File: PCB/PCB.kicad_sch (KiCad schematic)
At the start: 17 parts, among them J1 Conn_01x06_Female, J3 DB25_Receptacle_MountingHoles, U13 74HC165, U15 LT3042xMSE, U16 74HC165

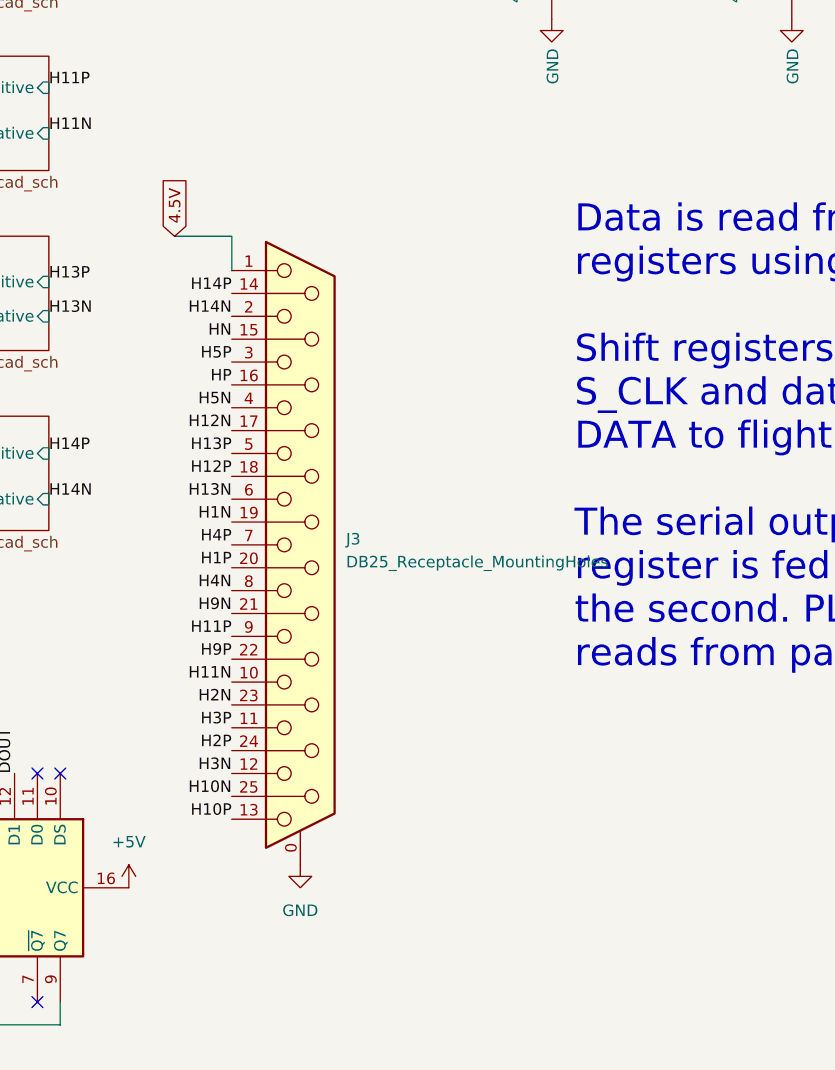
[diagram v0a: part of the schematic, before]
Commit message: Beginning new layout
As I am placing components on the board, I am getting the impression that 70 mm by 70 mm is too small of a board for what I am attempting. The through hole connectors that I am looking at are too big to allow 2 hx711 adc to fit alongside them in their current setup. At some point, I will have to go back to the circular pcb design but learn my lessons from it and set it up with the hx711's at 45 degrees and I may have enough room.
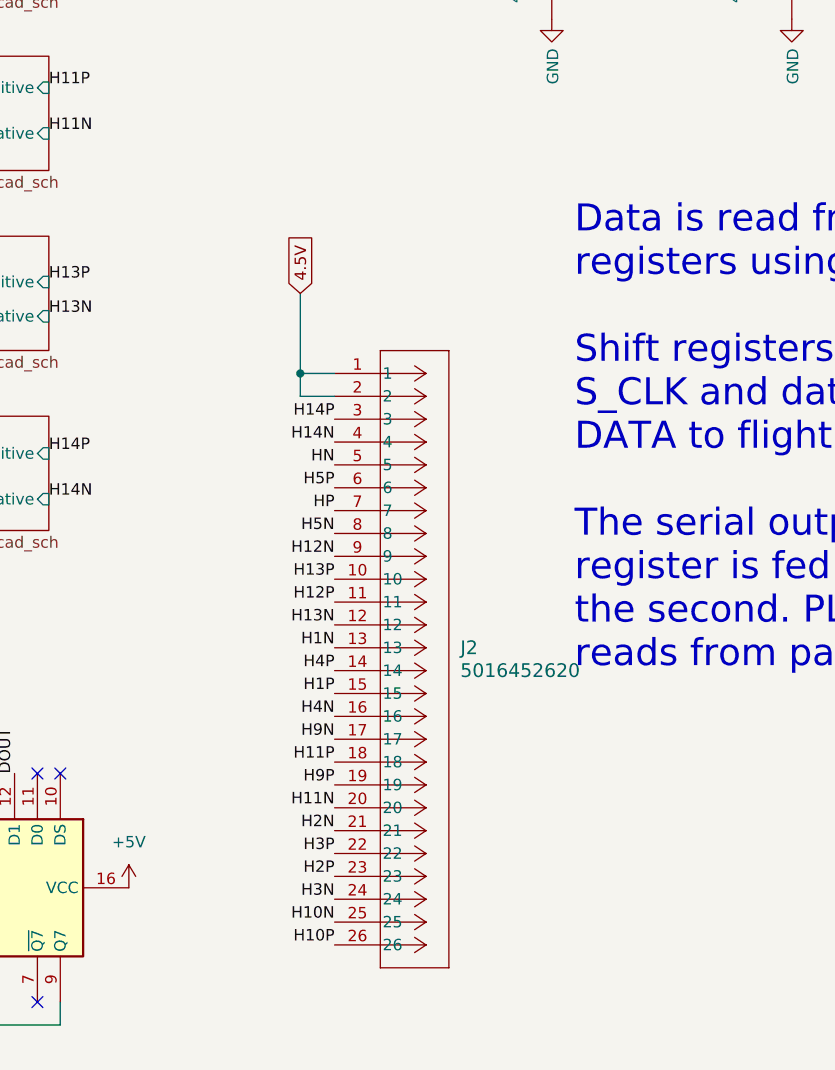
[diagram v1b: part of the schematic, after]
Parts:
- removed J3: DB25_Receptacle_MountingHoles, Connector_Dsub:DSUB-25_Female_Vertical_P2.77x2.84mm_MountingHoles, symbol Connector:DB25_Receptacle_MountingHoles
- added J2: 5016452620, Library:CON_5016452620_MOL, symbol 2024-03-05_00-01-19:5016452620
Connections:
- net 4.5V: now also J2.1, J2.2
- net H10N: now also J2.25
- net H10P: now also J2.26
- net H11N: now also J2.20
- net H11P: now also J2.18
- net H12N: now also J2.9
- net H12P: now also J2.11
- net H13N: now also J2.12
- net H13P: now also J2.10
- net H14N: now also J2.4
- net H14P: now also J2.3
- net H1N: now also J2.13
- net H1P: now also J2.15
- net H2N: now also J2.21
- net H2P: now also J2.23
- net H3N: now also J2.24
- net H3P: now also J2.22
- net H4N: now also J2.16
- net H4P: now also J2.14
- net H5N: now also J2.8
- net H5P: now also J2.6
- net H9N: now also J2.17
- net H9P: now also J2.19
- net HN: now also J2.5
- net HP: now also J2.7

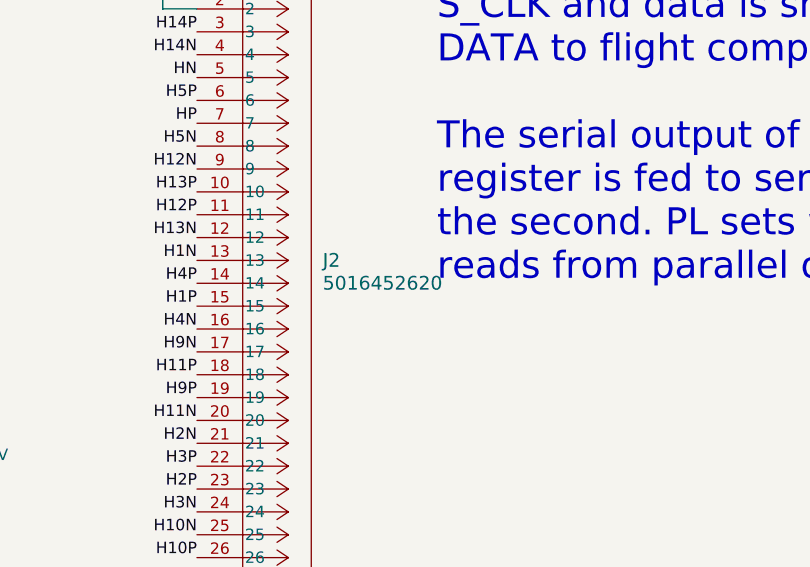
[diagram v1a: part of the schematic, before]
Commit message: Imported other downloaded connector
Imported other downloaded through hole connector to compare sizes with another one, even though they will be on different sides from the top of the board. I'm just concerned that I won't be able to work this board setup.
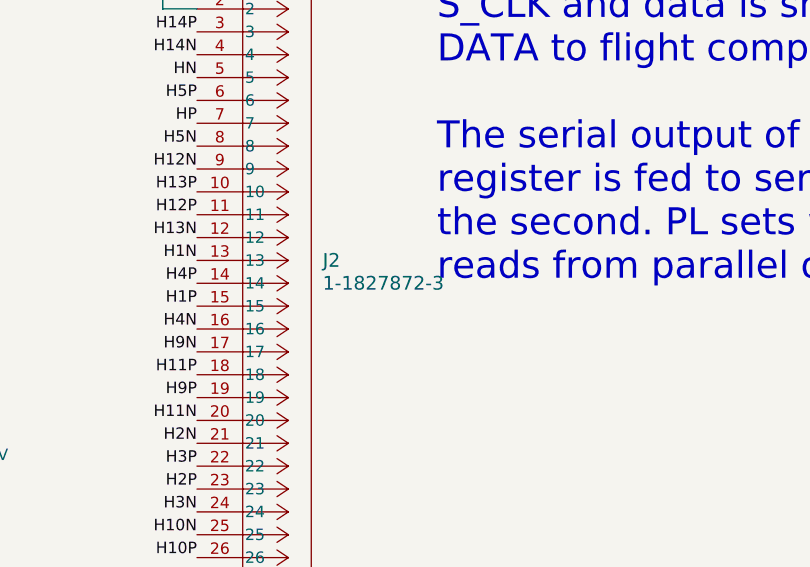
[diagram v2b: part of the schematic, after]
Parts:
- removed J2: 5016452620, Library:CON_5016452620_MOL, symbol 2024-03-05_00-01-19:5016452620
- added J2: 1-1827872-3, Library:CONN_1-1827872-3_TYC, symbol 2024-03-04_23-53-42:1-1827872-3
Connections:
- net 4.5V: now also J2.1, J2.2
- net H10N: now also J2.25
- net H10P: now also J2.26
- net H11N: now also J2.20
- net H11P: now also J2.18
- net H12N: now also J2.9
- net H12P: now also J2.11
- net H13N: now also J2.12
- net H13P: now also J2.10
- net H14N: now also J2.4
- net H14P: now also J2.3
- net H1N: now also J2.13
- net H1P: now also J2.15
- net H2N: now also J2.21
- net H2P: now also J2.23
- net H3N: now also J2.24
- net H3P: now also J2.22
- net H4N: now also J2.16
- net H4P: now also J2.14
- net H5N: now also J2.8
- net H5P: now also J2.6
- net H9N: now also J2.17
- net H9P: now also J2.19
- net HN: now also J2.5
- net HP: now also J2.7
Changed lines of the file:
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@@
-	)
-	(symbol
-		(lib_id "2024-03-05_00-01-19:5016452620")
-		(at 144.78 120.65 0)
-		(unit 1)
-		(exclude_from_sim no)
-		(in_bom yes)
-		(on_board yes)
-		(dnp no)
-		(fields_autoplaced yes)
-		(property "Reference" "J2"
-			(at 158.75 151.1299 0)
-			(effects
-				(font
-					(size 1.524 1.524)
-				)
-				(justify left)
-			)
-		)
-		(property "Value" "5016452620"
-			(at 158.75 153.6699 0)
-			(effects
-				(font
-					(size 1.524 1.524)
-				)
-				(justify left)
-			)
-		)
-		(property "Footprint" "Library:CON_5016452620_MOL"
-			(at 144.78 120.65 0)
-			(effects
-				(font
-					(size 1.27 1.27)
-					(italic yes)
-				)
-				(hide yes)
-			)
-		)
-		(property "Datasheet" "5016452620"
-			(at 144.78 120.65 0)
-			(effects
-				(font
-					(size 1.27 1.27)
-					(italic yes)
-				)
-				(hide yes)
-			)
-		)
-		(property "Description" ""
-			(at 144.78 120.65 0)
-			(effects
-				(font
-					(size 1.27 1.27)
-				)
-				(hide yes)
-			)
-		)
-		(pin "22"
-		)
-		(pin "13"
-		)
-		(pin "25"
-		)
-		(pin "20"
-		)
-		(pin "9"
-		)
-		(pin "21"
-		)
-		(pin "17"
-		)
-		(pin "14"
-		)
-		(pin "7"
-		)
-		(pin "26"
-		)
-		(pin "6"
-		)
-		(pin "18"
-		)
-		(pin "2"
-		)
-		(pin "5"
-		)
-		(pin "19"
-		)
-		(pin "15"
-		)
-		(pin "1"
-		)
-		(pin "8"
-		)
-		(pin "3"
-		)
-		(pin "4"
-		)
-		(pin "11"
-		)
-		(pin "24"
-		)
-		(pin "23"
-		)
-		(pin "10"
-		)
-		(pin "16"
-		)
-		(pin "12"
-		)
-		(instances
-			(project "PCB"
-				(path "/b6270a28-e0d9-4655-a18a-03dbf007b940"
-					(reference "J2")
-					(unit 1)
-				)
-			)
-		)
 	)
 	(symbol
@@
 					(unit 1)
 				)
+			)
+		)
+	)
+	(symbol
+		(lib_id "2024-03-04_23-53-42:1-1827872-3")
+		(at 144.78 120.65 0)
+		(unit 1)
+		(exclude_from_sim no)
+		(in_bom yes)
+		(on_board yes)
+		(dnp no)
+		(fields_autoplaced yes)
+		(property "Reference" "J2"
+			(at 158.75 151.1299 0)
+			(effects
+				(font
+					(size 1.524 1.524)
+				)
+				(justify left)
+			)
+		)
+		(property "Value" "1-1827872-3"
+			(at 158.75 153.6699 0)
+			(effects
+				(font
+					(size 1.524 1.524)
+				)
+				(justify left)
+			)
+		)
+		(property "Footprint" "Library:CONN_1-1827872-3_TYC"
+			(at 144.78 120.65 0)
+			(effects
+				(font
+					(size 1.27 1.27)
+					(italic yes)
+				)
+				(hide yes)
+			)
+		)
+		(property "Datasheet" "1-1827872-3"
+			(at 144.78 120.65 0)
+			(effects
+				(font
+					(size 1.27 1.27)
+					(italic yes)
+				)
+				(hide yes)
+			)
+		)
+		(property "Description" ""
+			(at 144.78 120.65 0)
+			(effects
+				(font
+					(size 1.27 1.27)
+				)
+				(hide yes)
+			)
+		)
+		(pin "14"
+		)
+		(pin "15"
+		)
+		(pin "12"
+		)
+		(pin "2"
+		)
+		(pin "1"
+		)
+		(pin "17"
+		)
+		(pin "11"
+		)
+		(pin "22"
+		)
+		(pin "25"
+		)
+		(pin "13"
+		)
+		(pin "24"
+		)
+		(pin "7"
+		)
+		(pin "23"
+		)
+		(pin "10"
+		)
+		(pin "3"
+		)
+		(pin "16"
+		)
+		(pin "18"
+		)
+		(pin "19"
+		)
+		(pin "26"
+		)
+		(pin "4"
+		)
+		(pin "5"
+		)
+		(pin "8"
+		)
+		(pin "20"
+		)
+		(pin "21"
+		)
+		(pin "9"
+		)
+		(pin "6"
+		)
+		(instances
+			(project "PCB"
+				(path "/b6270a28-e0d9-4655-a18a-03dbf007b940"
+					(reference "J2")
+					(unit 1)
+				)

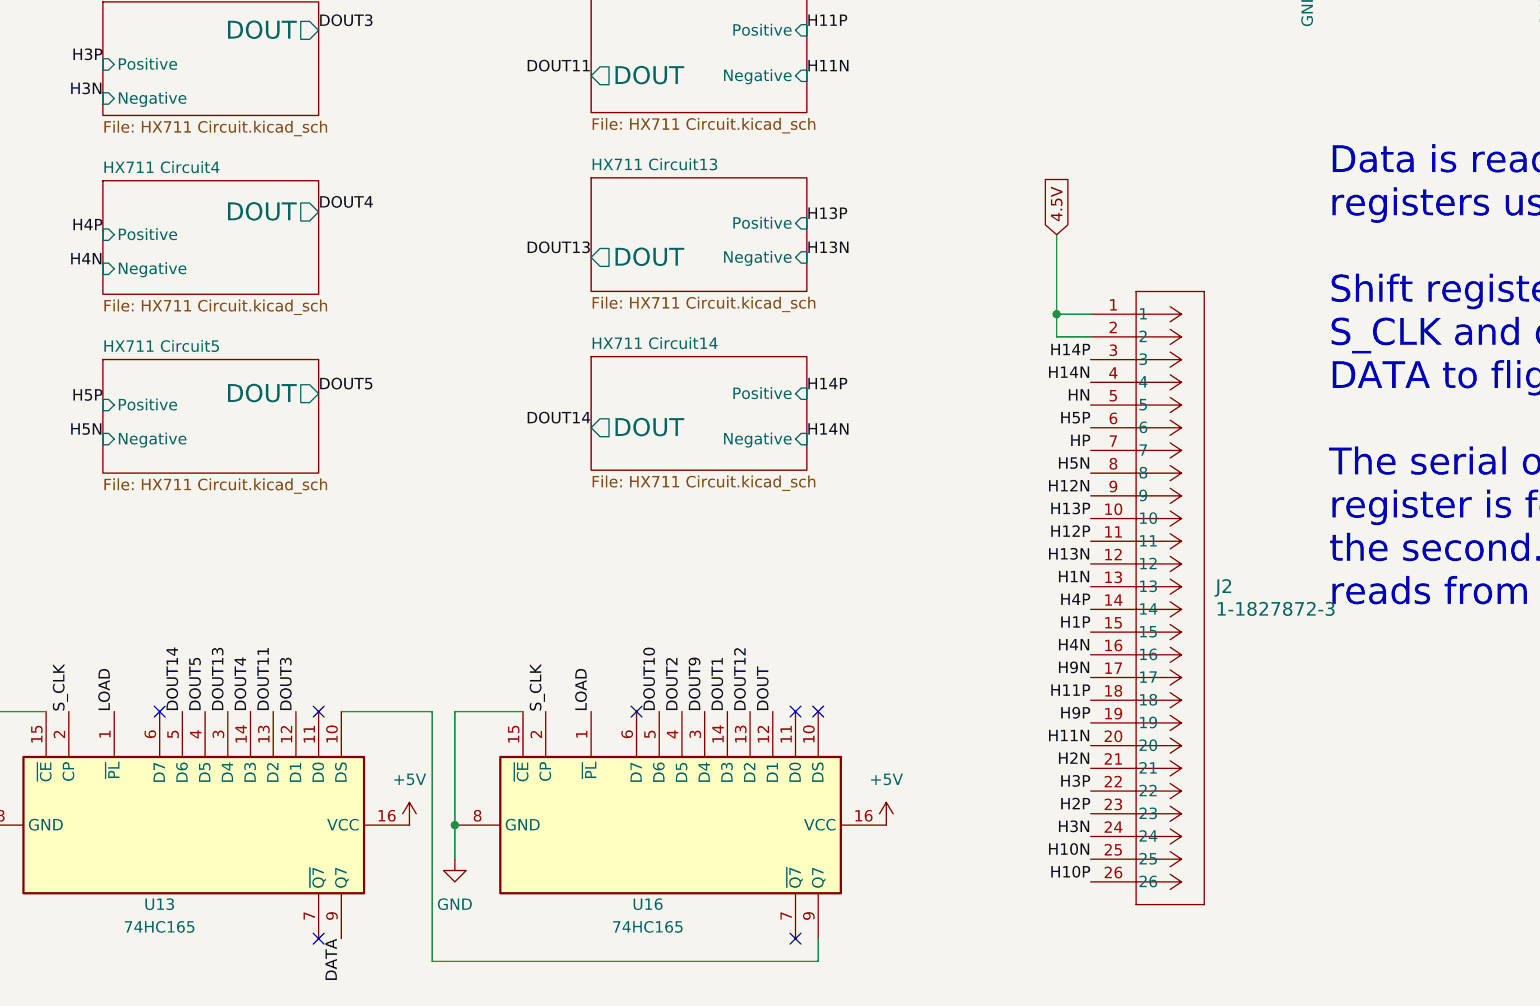
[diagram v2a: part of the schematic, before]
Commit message: Changed size of pcb
PCB size increased by 725 square mm by increasing size to a 75 mm by 75 mm square. Dout and the clock for the hx711s have been wired as well as the control wires for the shift registers.
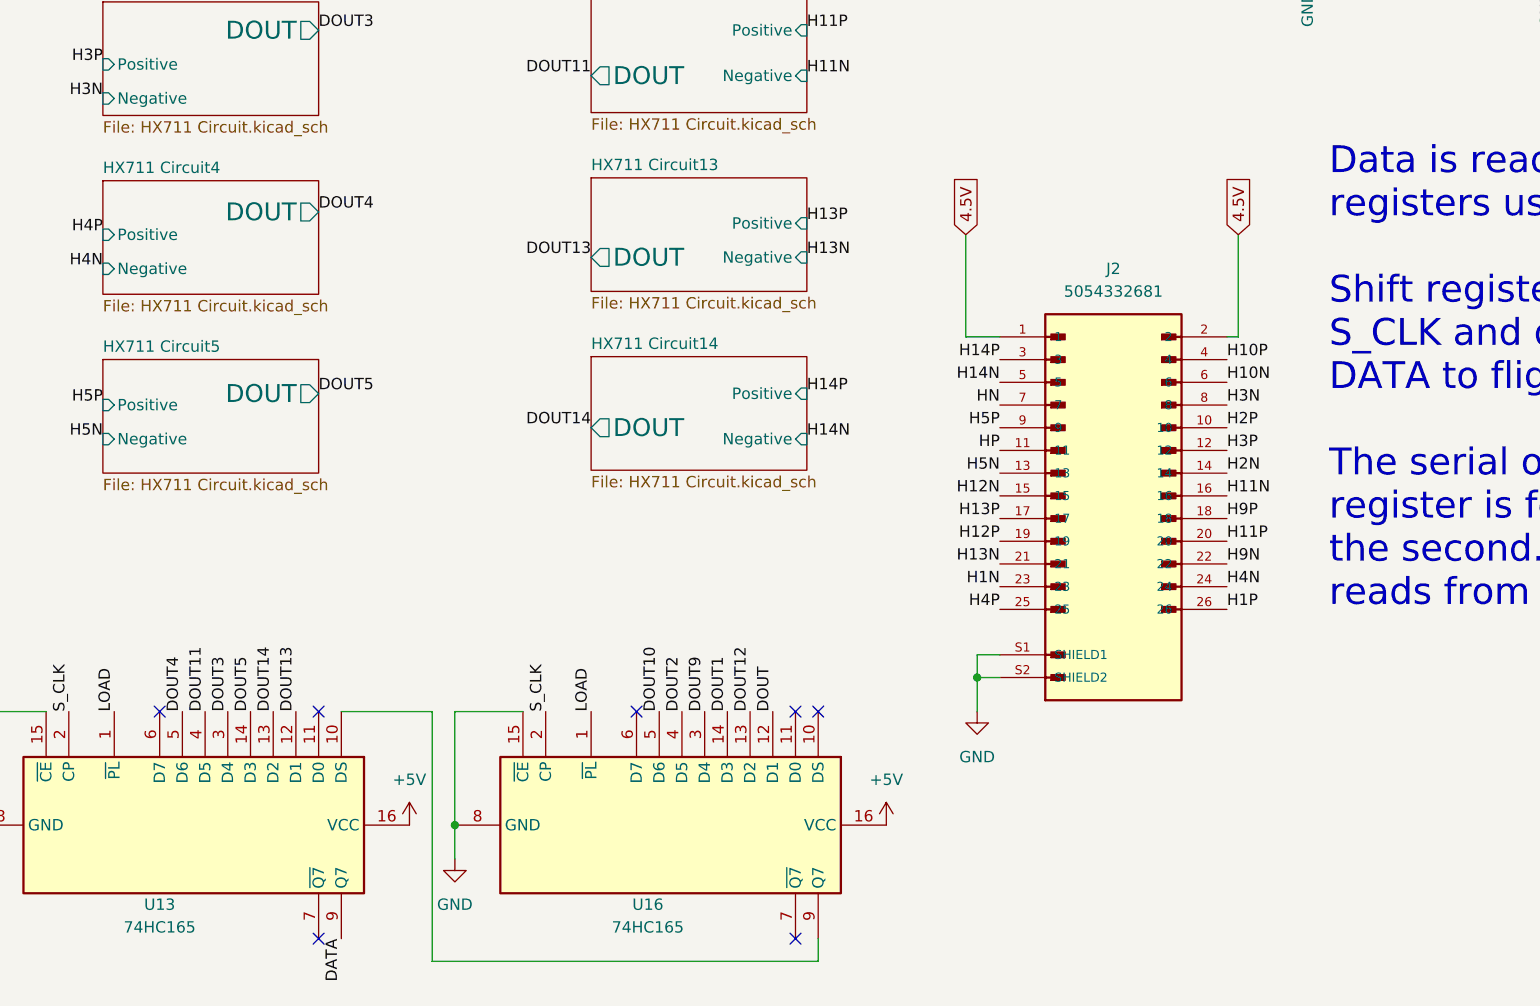
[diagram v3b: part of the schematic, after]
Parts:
- removed J2: 1-1827872-3, Library:CONN_1-1827872-3_TYC, symbol 2024-03-04_23-53-42:1-1827872-3
- added J2: 5054332681, 5054332681 (1):MOLEX_5054332681, symbol 5054332681:5054332681
- C25, C26, C27: footprint Capacitor_SMD:C_0805_2012Metric_Pad1.18x1.45mm_HandSolder -> Capacitor_SMD:C_0603_1608Metric_Pad1.08x0.95mm_HandSolder
- R37, R38, R39, R40: footprint Resistor_SMD:R_0805_2012Metric_Pad1.20x1.40mm_HandSolder -> Resistor_SMD:R_0603_1608Metric_Pad0.98x0.95mm_HandSolder
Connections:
- net 4.5V: now also J2.1, J2.2
- net DOUT11: now also U13.4 (D5); no longer U13.13 (D2)
- net DOUT13: now also U13.12 (D1); no longer U13.3 (D4)
- net DOUT14: now also U13.13 (D2); no longer U13.5 (D6)
- net DOUT3: now also U13.3 (D4); no longer U13.12 (D1)
- net DOUT4: now also U13.5 (D6); no longer U13.14 (D3)
- net DOUT5: now also U13.14 (D3); no longer U13.4 (D5)
- net GND: now also J2.S1 (SHIELD1), J2.S2 (SHIELD2)
- net H10N: now also J2.6
- net H10P: now also J2.4
- net H11N: now also J2.16
- net H11P: now also J2.20
- net H12N: now also J2.15
- net H12P: now also J2.19
- net H13N: now also J2.21
- net H13P: now also J2.17
- net H14N: now also J2.5
- net H14P: now also J2.3
- net H1N: now also J2.23
- net H1P: now also J2.26
- net H2N: now also J2.14
- net H2P: now also J2.10
- net H3N: now also J2.8
- net H3P: now also J2.12
- net H4N: now also J2.24
- net H4P: now also J2.25
- net H5N: now also J2.13
- net H5P: now also J2.9
- net H9N: now also J2.22
- net H9P: now also J2.18
- net HN: now also J2.7
- net HP: now also J2.11
